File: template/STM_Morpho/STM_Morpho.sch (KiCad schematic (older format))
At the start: 2 parts, among them CN10 CONN_02X19, CN7 CONN_02X19

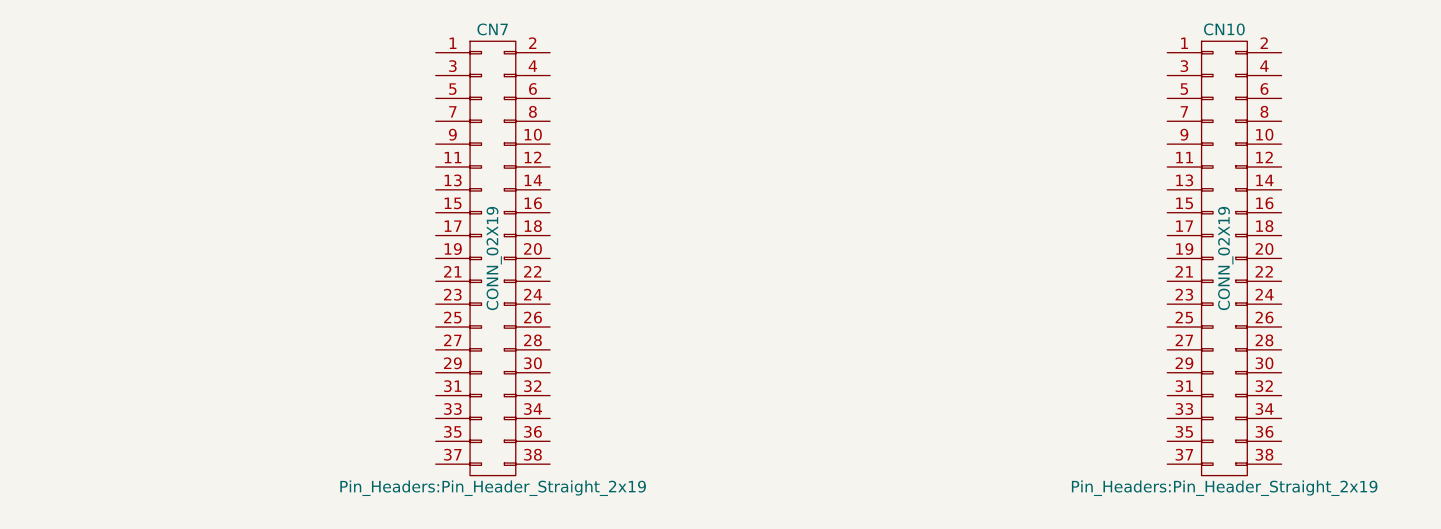
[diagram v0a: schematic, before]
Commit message: Update for KiCaD 5.1.7
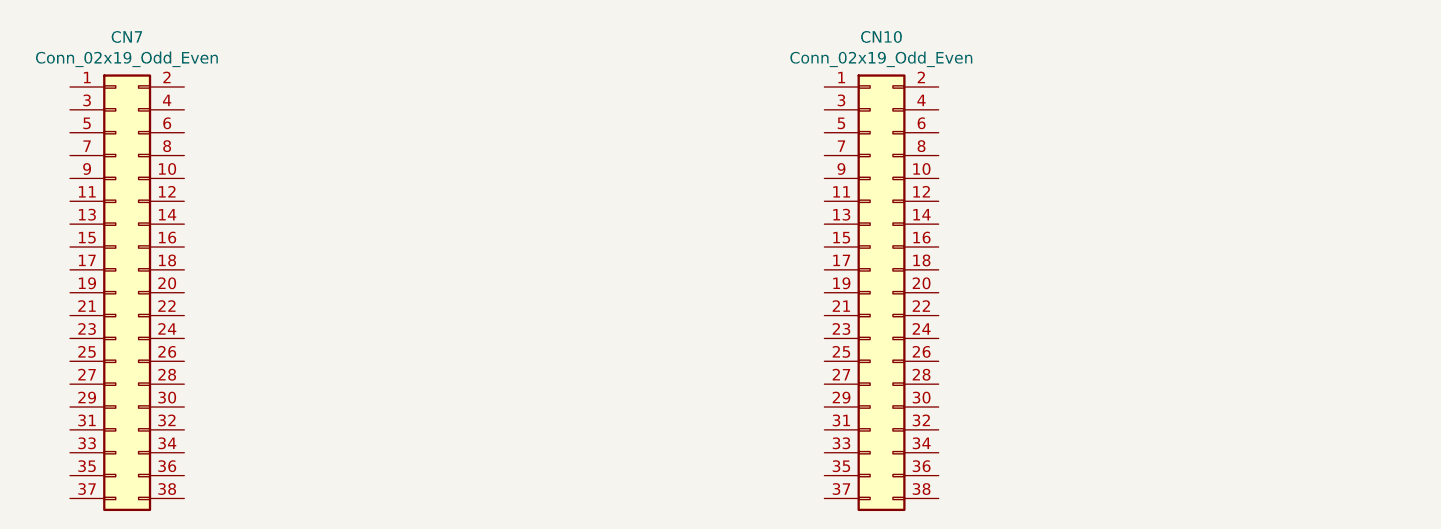
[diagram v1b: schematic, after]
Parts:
- removed CN10, CN7: CONN_02X19, Pin_Headers:Pin_Header_Straight_2x19, symbol CONN_02X19
- added CN10, CN7: Conn_02x19_Odd_Even, Connector_PinSocket_2.54mm:PinSocket_2x19_P2.54mm_Vertical, symbol Connector_Generic:Conn_02x19_Odd_Even
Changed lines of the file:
@@
-EESchema Schematic File Version 2
-LIBS:power
-LIBS:device
-LIBS:transistors
-LIBS:conn
-LIBS:linear
-LIBS:regul
-LIBS:74xx
-LIBS:cmos4000
-LIBS:adc-dac
-LIBS:memory
-LIBS:xilinx
-LIBS:microcontrollers
-LIBS:dsp
-LIBS:microchip
-LIBS:analog_switches
-LIBS:motorola
-LIBS:texas
-LIBS:intel
-LIBS:audio
-LIBS:interface
-LIBS:digital-audio
-LIBS:philips
-LIBS:display
-LIBS:cypress
-LIBS:siliconi
-LIBS:opto
-LIBS:atmel
-LIBS:contrib
-LIBS:valves
-EELAYER 25 0
+EESchema Schematic File Version 4
+EELAYER 30 0
 EELAYER END
 $Descr A4 11693 8268
@@
 $EndDescr
 $Comp
-L CONN_02X19 CN7
-U 1 1 58745202
-P 3550 3050
-F 0 "CN7" H 3550 4050 50  0000 C CNN
-F 1 "CONN_02X19" V 3550 3050 50  0000 C CNN
-F 2 "Pin_Headers:Pin_Header_Straight_2x19" H 3550 2050 50  0000 C CNN
-F 3 "" H 3550 2050 50  0000 C CNN
-	1    3550 3050
+L Connector_Generic:Conn_02x19_Odd_Even CN7
+U 1 1 5F9F2DD0
+P 1900 3200
+F 0 "CN7" H 1950 4317 50  0000 C CNN
+F 1 "Conn_02x19_Odd_Even" H 1950 4226 50  0000 C CNN
+F 2 "Connector_PinSocket_2.54mm:PinSocket_2x19_P2.54mm_Vertical" H 1900 3200 50  0001 C CNN
+F 3 "~" H 1900 3200 50  0001 C CNN
+	1    1900 3200
 	1    0    0    -1
 $EndComp
 $Comp
-L CONN_02X19 CN10
-U 1 1 5874523E
-P 6750 3050
-F 0 "CN10" H 6750 4050 50  0000 C CNN
-F 1 "CONN_02X19" V 6750 3050 50  0000 C CNN
-F 2 "Pin_Headers:Pin_Header_Straight_2x19" H 6750 2050 50  0000 C CNN
-F 3 "" H 6750 2050 50  0000 C CNN
-	1    6750 3050
+L Connector_Generic:Conn_02x19_Odd_Even CN10
+U 1 1 5F9F448E
+P 5200 3200
+F 0 "CN10" H 5250 4317 50  0000 C CNN
+F 1 "Conn_02x19_Odd_Even" H 5250 4226 50  0000 C CNN
+F 2 "Connector_PinSocket_2.54mm:PinSocket_2x19_P2.54mm_Vertical" H 5200 3200 50  0001 C CNN
+F 3 "~" H 5200 3200 50  0001 C CNN
+	1    5200 3200
 	1    0    0    -1
 $EndComp
